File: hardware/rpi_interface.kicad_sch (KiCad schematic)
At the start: 3 parts, among them J14 RPI_Connector

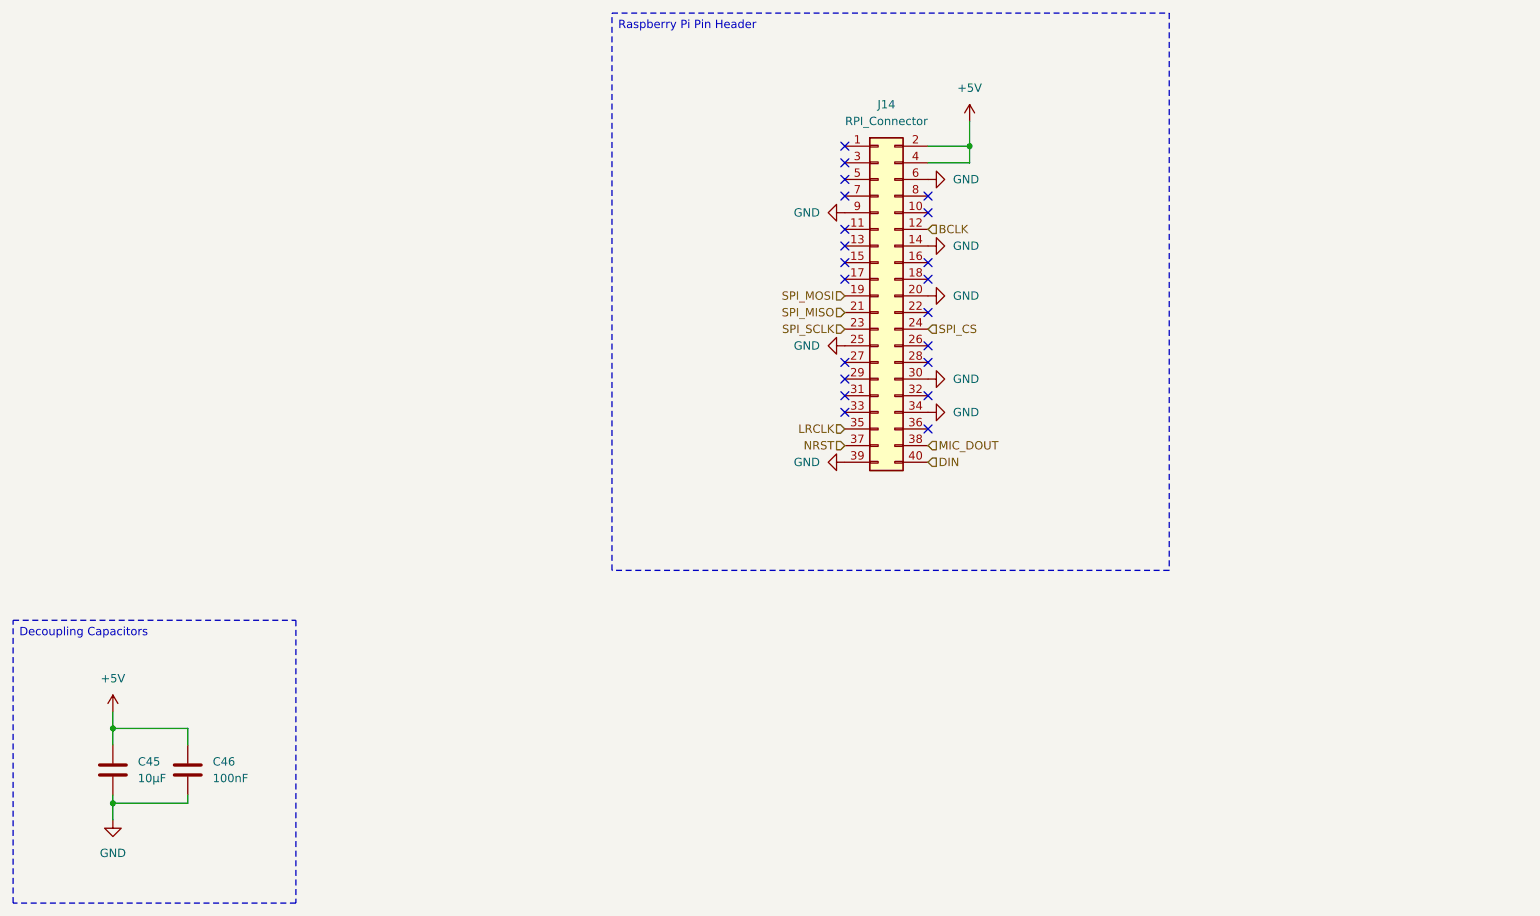
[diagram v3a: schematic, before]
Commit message: Adding cooling fan
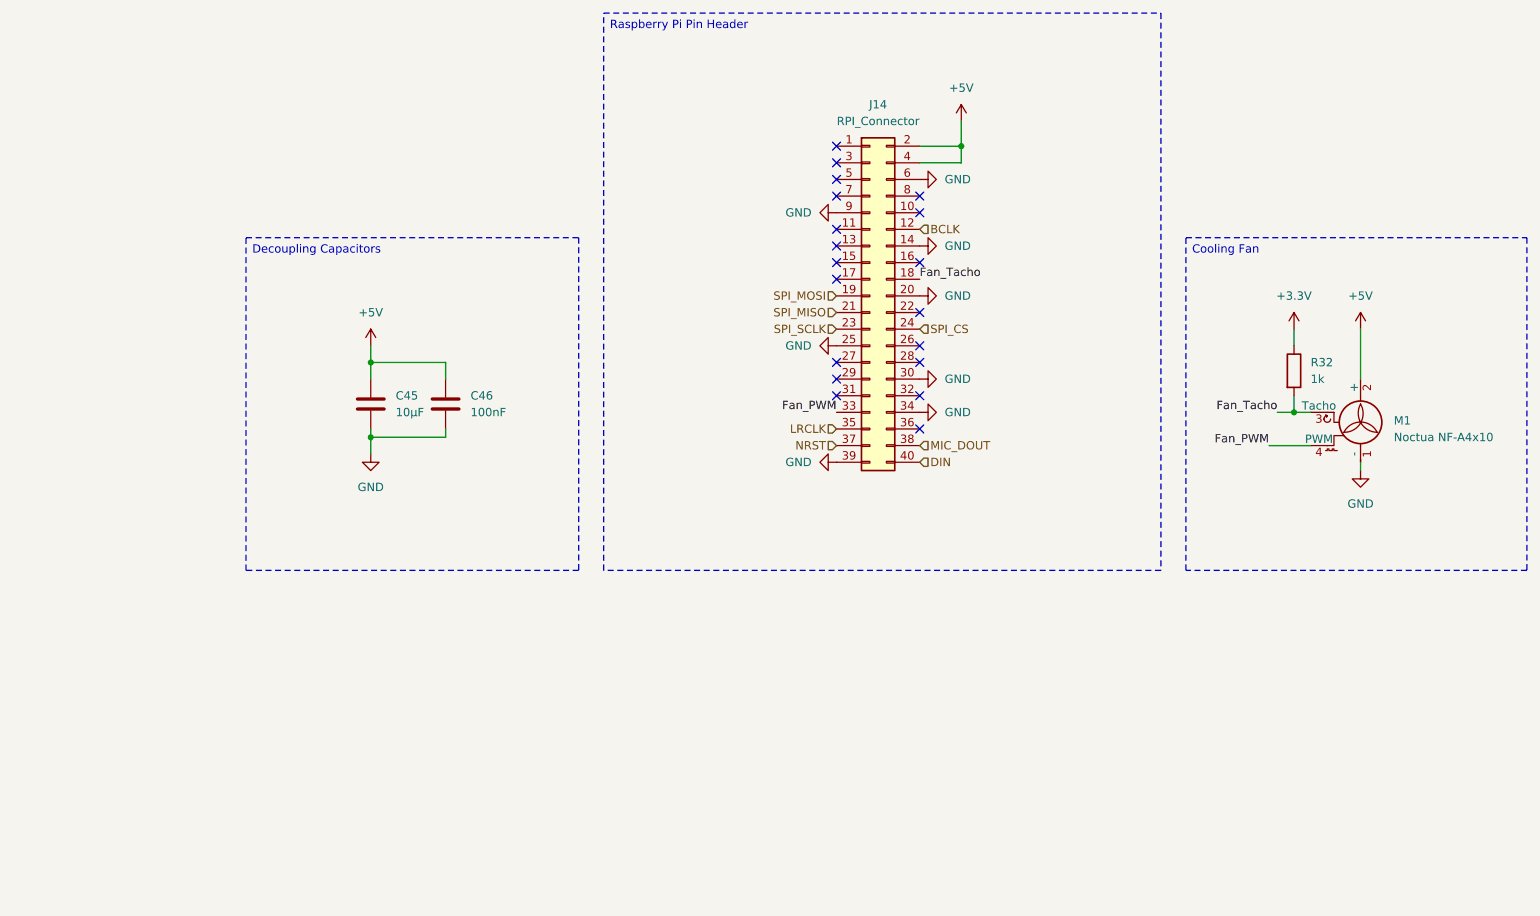
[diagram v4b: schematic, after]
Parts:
- added M1: Noctua NF-A4x10, symbol Motor:Fan_4pin
- added R32: 1k, symbol Device:R
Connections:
- net +5V: now also M1.2 (+)
- net GND: now also M1.1 (-)
- net Fan_Tacho: now reaches J14.18 (Pin_18)
- net Fan_Tacho: now also M1.3 (Tacho), R32.2
- net Fan_PWM: now reaches J14.33 (Pin_33)
- net Fan_PWM: now also M1.4 (PWM)
- new net +3.3V: R32.1
- no-connect marks 21 -> 19
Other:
- moved on the sheet: C45, C46, J14

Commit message: Adding footprints
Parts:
- J14: footprint (none) -> Connector_PinSocket_2.54mm:PinSocket_2x20_P2.54mm_Vertical
- M1: footprint (none) -> Connector:FanPinHeader_1x04_P2.54mm_Vertical
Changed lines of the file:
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@@
 			)
 		)
-		(property "Footprint" ""
+		(property "Footprint" "Connector_PinSocket_2.54mm:PinSocket_2x20_P2.54mm_Vertical"
 			(at 147.32 100.33 0)
 			(effects
@@
 			)
 		)
-		(property "Footprint" ""
+		(property "Footprint" "Connector:FanPinHeader_1x04_P2.54mm_Vertical"
 			(at 222.25 120.396 0)
 			(effects

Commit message: Updating footprints
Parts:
- C45: footprint (none) -> Capacitor_SMD:C_0805_2012Metric
- C46: footprint (none) -> Capacitor_SMD:C_0603_1608Metric
- R32: footprint (none) -> Resistor_SMD:R_0603_1608Metric
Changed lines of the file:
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@@
 			)
 		)
-		(property "Footprint" ""
+		(property "Footprint" "Capacitor_SMD:C_0603_1608Metric"
 			(at 83.5152 120.65 0)
 			(effects
@@
 			)
 		)
-		(property "Footprint" ""
+		(property "Footprint" "Resistor_SMD:R_0603_1608Metric"
 			(at 210.312 111.76 90)
 			(effects
@@
 			)
 		)
-		(property "Footprint" ""
+		(property "Footprint" "Capacitor_SMD:C_0805_2012Metric"
 			(at 72.0852 120.65 0)
 			(effects

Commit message: Modyfing components footprints
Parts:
- C46: footprint Capacitor_SMD:C_0603_1608Metric -> Capacitor_SMD:C_0402_1005Metric
- R32: footprint Resistor_SMD:R_0603_1608Metric -> Resistor_SMD:R_0402_1005Metric
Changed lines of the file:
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@@
 			)
 		)
-		(property "Footprint" "Capacitor_SMD:C_0603_1608Metric"
+		(property "Footprint" "Capacitor_SMD:C_0402_1005Metric"
 			(at 83.5152 120.65 0)
 			(effects
@@
 			)
 		)
+		(property "Sim.Device" ""
+			(at 82.55 116.84 0)
+			(effects
+				(font
+					(size 1.27 1.27)
+				)
+				(hide yes)
+			)
+		)
+		(property "Sim.Type" ""
+			(at 82.55 116.84 0)
+			(effects
+				(font
+					(size 1.27 1.27)
+				)
+				(hide yes)
+			)
+		)
 		(pin "2"
 		)
@@
 			)
 		)
-		(property "Footprint" "Resistor_SMD:R_0603_1608Metric"
+		(property "Footprint" "Resistor_SMD:R_0402_1005Metric"
 			(at 210.312 111.76 90)
 			(effects
@@
 			)
 		)
+		(property "Sim.Device" ""
+			(at 212.09 111.76 0)
+			(effects
+				(font
+					(size 1.27 1.27)
+				)
+				(hide yes)
+			)
+		)
+		(property "Sim.Type" ""
+			(at 212.09 111.76 0)
+			(effects
+				(font
+					(size 1.27 1.27)
+				)
+				(hide yes)
+			)
+		)
 		(pin "2"
 		)
@@
 			)
 		)
+		(property "Sim.Device" ""
+			(at 147.32 100.33 0)
+			(effects
+				(font
+					(size 1.27 1.27)
+				)
+				(hide yes)
+			)
+		)
+		(property "Sim.Type" ""
+			(at 147.32 100.33 0)
+			(effects
+				(font
+					(size 1.27 1.27)
+				)
+				(hide yes)
+			)
+		)
 		(pin "14"
 		)
@@
 			)
 		)
+		(property "Sim.Device" ""
+			(at 222.25 120.65 0)
+			(effects
+				(font
+					(size 1.27 1.27)
+				)
+				(hide yes)
+			)
+		)
+		(property "Sim.Type" ""
+			(at 222.25 120.65 0)
+			(effects
+				(font
+					(size 1.27 1.27)
+				)
+				(hide yes)
+			)
+		)
 		(pin "1"
 		)
@@
 			(at 71.12 116.84 0)
 			(effects
+				(font
+					(size 1.27 1.27)
+				)
+				(hide yes)
+			)
+		)
+		(property "Sim.Device" ""
+			(at 71.12 116.84 0)
+			(effects
+				(font
+					(size 1.27 1.27)
+				)
+				(hide yes)
+			)
+		)
+		(property "Sim.Type" ""
+			(at 71.12 116.84 0)
+			(effects

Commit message: Updating component placement
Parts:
- C45: footprint Capacitor_SMD:C_0805_2012Metric -> Capacitor_SMD:CP_Elec_4x4.5
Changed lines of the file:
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@@
 			)
 		)
-		(property "Footprint" "Capacitor_SMD:C_0805_2012Metric"
+		(property "Footprint" "Capacitor_SMD:CP_Elec_4x4.5"
 			(at 72.0852 120.65 0)
 			(effects
